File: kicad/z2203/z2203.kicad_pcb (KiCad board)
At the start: 4 copper layers, 80 x 80 mm, 21 parts, among them J1 Conn_01x01, J2 Conn_01x02, J3 Conn_02x20_Odd_Even, U13 LM4040AIM3-2.5, U14 AD5328, U15 M24C02-WMN, U7 PCA9555D

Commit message: routed z2203
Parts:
- removed C13, C25, C39: 0.1u, Capacitor_SMD:C_0603_1608Metric
- removed C24: 4.7u, Capacitor_SMD:C_0805_2012Metric
- removed R47: 4k7, Resistor_SMD:R_1206_3216Metric
- removed U13: LM4040AIM3-2.5, Package_TO_SOT_SMD:SOT-23
- removed U14: AD5328, Package_SO:TSSOP-16_4.4x5mm_P0.65mm
- added C1: 0.1u, Capacitor_SMD:C_0603_1608Metric, F.Cu at (77.2, 51.2)
- added C10: 0.1u, Capacitor_SMD:C_0603_1608Metric, F.Cu at (122.0, 59.0)
- added C2: 0.1u, Capacitor_SMD:C_0603_1608Metric, F.Cu at (92.4, 54.6)
- added C3: 0.1u, Capacitor_SMD:C_0603_1608Metric, F.Cu at (140.0, 76.3)
- added C4: 0.1u, Capacitor_SMD:C_0603_1608Metric, F.Cu at (142.2, 40.2)
- added C6: 0.1u, Capacitor_SMD:C_0603_1608Metric, F.Cu at (132.0, 52.4)
- added C7: 0.1u, Capacitor_SMD:C_0603_1608Metric, F.Cu at (76.6, 78.8)
- added C8: 0.1u, Capacitor_SMD:C_0603_1608Metric, F.Cu at (76.6, 66.8)
- added C9: 10u, Capacitor_SMD:C_0805_2012Metric, F.Cu at (79.0, 66.6)
- added D1: LED, LED_SMD:LED_0603_1608Metric, F.Cu at (143.6, 69.2)
- added R1: 4k7, Resistor_SMD:R_0603_1608Metric, F.Cu at (142.8, 72.8)
- added R2: 51, Resistor_SMD:R_0603_1608Metric, F.Cu at (79.0, 78.8)
- added R3: 47k, Resistor_SMD:R_0603_1608Metric, F.Cu at (74.0, 61.8)
- added R4: 47k, Resistor_SMD:R_0603_1608Metric, F.Cu at (74.0, 63.8)
- added R5: 47k, Resistor_SMD:R_0603_1608Metric, F.Cu at (74.0, 65.8)
- added R6: 47k, Resistor_SMD:R_0603_1608Metric, F.Cu at (71.4, 72.8)
- added R7: 47k, Resistor_SMD:R_0603_1608Metric, F.Cu at (73.8, 78.0)
- added R8: 51, Resistor_SMD:R_0603_1608Metric, F.Cu at (73.8, 80.0)
- added R9: 47k, Resistor_SMD:R_0603_1608Metric, F.Cu at (74.0, 67.6)
- added TP1: TestPoint, TestPoint:TestPoint_Pad_2.0x2.0mm, F.Cu at (121.2, 51.8)
- added TP11: TestPoint, TestPoint:TestPoint_Pad_2.0x2.0mm, F.Cu at (111.0, 52.2)
- added TP12: TestPoint, TestPoint:TestPoint_Pad_2.0x2.0mm, F.Cu at (69.2, 59.0)
- added TP2: TestPoint, TestPoint:TestPoint_Pad_2.0x2.0mm, F.Cu at (130.8, 48.4)
- added TP3: TestPoint, TestPoint:TestPoint_Pad_2.0x2.0mm, F.Cu at (131.8, 37.6)
- added TP4: TestPoint, TestPoint:TestPoint_Pad_2.0x2.0mm, F.Cu at (135.0, 64.4)
- added TP5: TestPoint, TestPoint:TestPoint_Pad_2.0x2.0mm, F.Cu at (139.1, 65.2)
- added TP6: TestPoint, TestPoint:TestPoint_Pad_2.0x2.0mm, F.Cu at (140.6, 50.9)
- added TP8: TestPoint, TestPoint:TestPoint_Pad_2.0x2.0mm, F.Cu at (136.8, 50.9)
- added TP9: TestPoint, TestPoint:TestPoint_Pad_2.0x2.0mm, F.Cu at (137.8, 79.8)
- added U1: YM2203, Package_DIP:DIP-40_W15.24mm, F.Cu at (126.3, 33.0)
- added U2: YM3014, Package_DIP:DIP-8_W7.62mm, F.Cu at (91.5, 57.0)
- added U3: 74HC595, Package_SO:TSSOP-16_4.4x5mm_P0.65mm, F.Cu at (137.2, 43.6)
- added U4: 74HC595, Package_SO:TSSOP-16_4.4x5mm_P0.65mm, F.Cu at (136.8, 71.0)
- added U6: TL074, Package_SO:TSSOP-14_4.4x5mm_P0.65mm, F.Cu at (76.4, 72.9)
- added X1: SX3M3.57, Oscillator:Oscillator_SMD_Abracon_ASE-4Pin_3.2x2.5mm, F.Cu at (122.0, 55.8)
- R56: value 2k -> 4k7
- U7: value PCA9555D -> 74HC00; footprint Package_SO:TSSOP-24_4.4x7.8mm_P0.65mm -> Package_SO:SOIC-14_3.9x8.7mm_P1.27mm
- moved J1 76.6 mm to (132.4, 28.6)
- moved G*** 76.3 mm to (69.4, 44.2), turned to 90 degrees
- moved D4 59.3 mm to (85.0, 27.7), turned to 180 degrees
- moved R56 57.3 mm to (88.7, 27.7), turned to 180 degrees
- moved U15 15.4 mm to (120.0, 78.5)
- moved C37 14.4 mm to (122.0, 84.4), turned to 90 degrees
- moved R20 8.86 mm to (142.2, 79.0)
- moved U7 5.65 mm to (136.8, 57.6), turned to 90 degrees
- moved J2 3.10 mm to (143.0, 83.3), turned to 0 degrees
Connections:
- D4 pad 1: Net-(D4-Pad1) -> Net-(D4-K)
- J3 pad 14: /GPIO_MODULE_DRIVEN -> unconnected-(J3-Pin_14-Pad14)
- J3 pad 21: /CARD1_OUT1 -> unconnected-(J3-Pin_21-Pad21)
- J3 pad 22: /CARD1_OUT2 -> unconnected-(J3-Pin_22-Pad22)
- J3 pad 23: /CARD2_OUT1 -> unconnected-(J3-Pin_23-Pad23)
- J3 pad 25: /CARD2_OUT2 -> unconnected-(J3-Pin_25-Pad25)
- J3 pad 26: /CARD3_OUT1 -> unconnected-(J3-Pin_26-Pad26)
- J3 pad 27: /CARD3_OUT2 -> unconnected-(J3-Pin_27-Pad27)
- J3 pad 29: /CARD4_OUT1 -> unconnected-(J3-Pin_29-Pad29)
- J3 pad 3: /SPI_MISO -> unconnected-(J3-Pin_3-Pad3)
- J3 pad 30: /CARD4_OUT2 -> unconnected-(J3-Pin_30-Pad30)
- J3 pad 31: /CARD5_OUT1 -> unconnected-(J3-Pin_31-Pad31)
- J3 pad 33: /CARD5_OUT2 -> unconnected-(J3-Pin_33-Pad33)
- J3 pad 34: /CARD6_OUT1 -> unconnected-(J3-Pin_34-Pad34)
- J3 pad 35: /CARD6_OUT2 -> unconnected-(J3-Pin_35-Pad35)
- J3 pad 37: /CARD7_OUT1 -> unconnected-(J3-Pin_37-Pad37)
- R56 pad 1: Net-(D4-Pad1) -> Net-(U1-IOA1)
- R56 pad 2: /LED_CTRL -> Net-(D4-K)
- U7 pad 1: unconnected-(U7-Pad1) -> +5V
- U7 pad 10: unconnected-(U7-Pad10) -> /CLK_CS1
- U7 pad 11: unconnected-(U7-Pad11) -> /CLK_CS1
- U7 pad 12: GND -> Net-(U7-Pad12)
- U7 pad 13: unconnected-(U7-Pad13) -> /SPI_CLK
- U7 pad 14: unconnected-(U7-Pad14) -> +5V
- U7 pad 2: /I2C_ADDR1 -> /SPI_CS1
- U7 pad 3: /I2C_ADDR2 -> Net-(U7-Pad12)
- U7 pad 7: /LED_CTRL -> GND
- U7 pad 8: unconnected-(U7-Pad8) -> /~CLK_CS1
- U7 pad 9: unconnected-(U7-Pad9) -> +5V
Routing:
- net +5V: track 21.5 -> 250.5 mm, vias 6 -> 11
- net /SPI_CS1: track 0.00 -> 74.7 mm
- net /YM2203_CLKS: track 0.00 -> 49.3 mm
- net -12V: track 0.00 -> 43.7 mm, vias 0 -> 1
- net +12V: track 0.00 -> 41.1 mm, vias 0 -> 1
- net /YM_CH_A: track 0.00 -> 38.1 mm
- net /YM_CH_B: track 0.00 -> 35.3 mm
- net /SPI_CS0: track 64.4 -> 30.4 mm
- net /YM_CH_C: track 0.00 -> 32.9 mm
- net /YM_D7: track 0.00 -> 31.3 mm
- net /YM_D6: track 0.00 -> 28.2 mm
- net /YM_A0: track 0.00 -> 27.9 mm, vias 0 -> 1
- net /YM_D5: track 0.00 -> 25.2 mm
- net Net-(U2-BUFF): track 0.00 -> 23.8 mm, vias 0 -> 1
- net /YM_D4: track 0.00 -> 22.4 mm
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- added copper zone on In2.Cu, net GND
- removed copper zone on In2.Cu, net +5V

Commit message: routed z2203
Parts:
- moved TP3 24.9 mm to (128.4, 70.0)
- moved C4 3.42 mm to (118.8, 57.8), turned to 90 degrees
- moved D1 0.19 mm to (85.2, 27.7)
- renumbered C3 to C10, C6 to C3, C10 to C4, C4 to C5, C9 to C6, C8 to C7, C7 to C8, C37 to C9, D4 to D1, D1 to D2, H4 to H1, H1 to H4, R56 to R1, R20 to R10, R1 to R11, R3 to R2, R8 to R3, R9 to R4, R4 to R5, R2 to R6, R5 to R8, R6 to R9, TP3 to TP1, TP9 to TP10, TP12 to TP2, TP11 to TP3, TP8 to TP4, TP1 to TP5, TP2 to TP6, TP6 to TP7, TP4 to TP8, TP5 to TP9, U7 to U3, U3 to U4, U6 to U5, U15 to U6, U4 to U7
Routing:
- net /YM2203_CLKS: track 49.3 -> 54.2 mm
- net +5V: track 250.5 -> 248.9 mm
- net Net-(U2-MP): track 19.2 -> 17.8 mm
- net GND: track 129.0 -> 127.8 mm
- net /SPI_CS1: track 74.7 -> 73.9 mm, vias 0 -> 1
- net /SPI_MOSI: track 60.9 -> 61.3 mm, vias 2 -> 0
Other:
- board text added: "TEST POINTS TP1 : YM D1 TP2 : YM CHANNEL A TP3 : SPI CS1 TP4 : CLK NAND CS1 TP5 : 3.57 MHZ CLK TP6 : YM D0 TP7 : CLK AND CS1 TP8 : YM A0 TP9 : SPI CS0 QB TP10 : SPI MOSI"
- board text added: "Z2203 FM SYNTH V0.1"

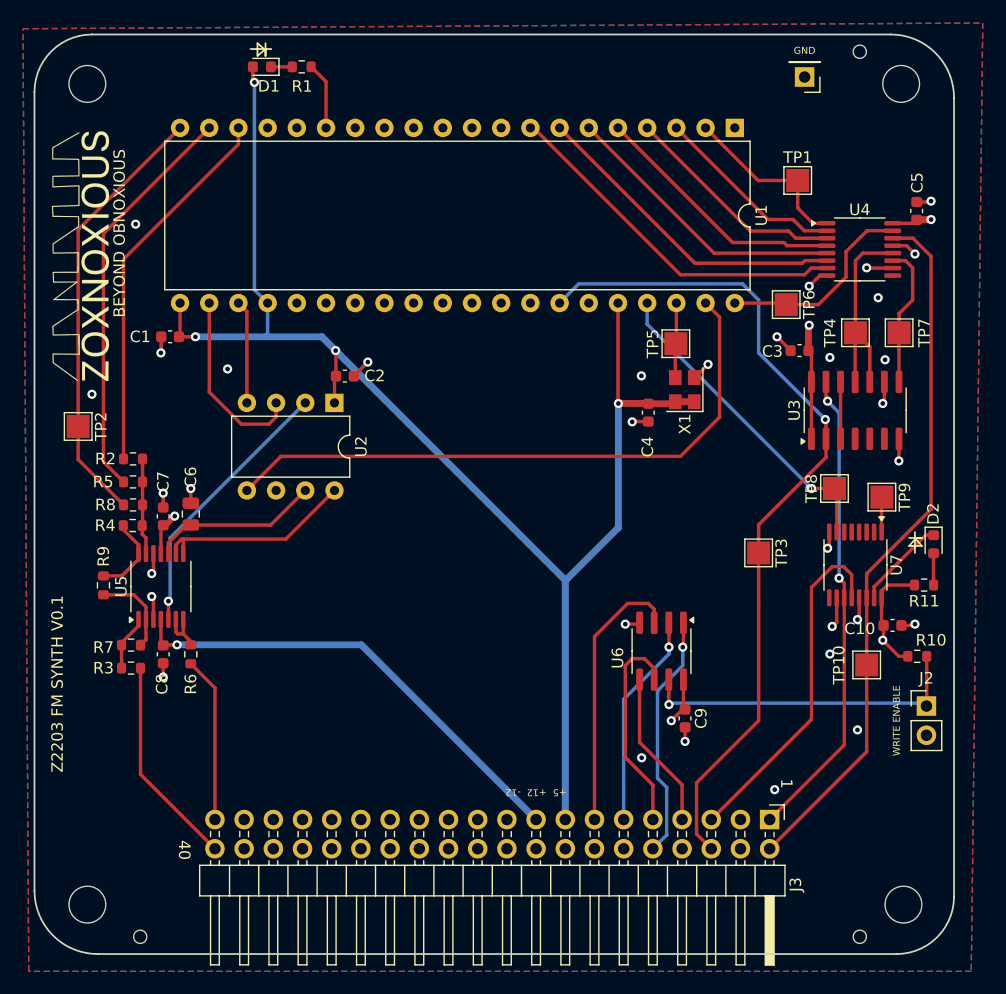
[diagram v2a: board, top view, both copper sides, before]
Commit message: move some stuff around for some minor changes.  The 2203 WR looks fine based on Capcom's Commando schematics
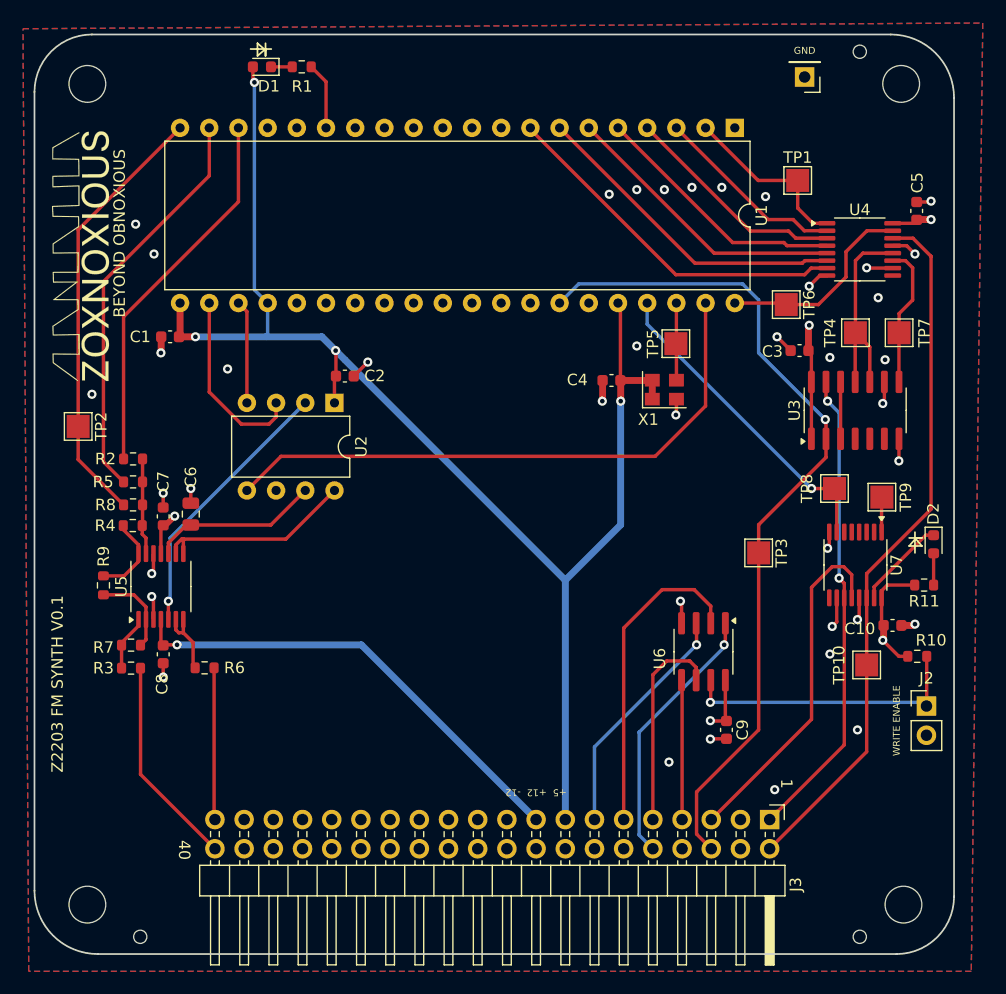
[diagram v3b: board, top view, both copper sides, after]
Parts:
- moved C4 4.25 mm to (115.6, 55.0), turned to 0 degrees
- moved C9 3.74 mm to (125.6, 85.4)
- moved U6 3.65 mm to (123.6, 78.6)
- moved X1 1.77 mm to (120.2, 55.8), turned to 0 degrees
- moved R6 1.68 mm to (80.2, 80.0), turned to 180 degrees
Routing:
- net /I2C_ADDR1: track 18.8 -> 27.7 mm, vias 1 -> 0
- net Net-(J2-Pin_1): track 29.0 -> 25.2 mm
- net /I2C_ADDR2: track 23.7 -> 20.8 mm, vias 0 -> 1
- net /YM2203_CLKS: track 54.2 -> 51.9 mm
- net Net-(U5B--): track 4.31 -> 6.30 mm
- net /I2C_ADDR0: track 21.4 -> 23.2 mm
- net /SDA1: track 13.7 -> 12.1 mm
- net /THIS_OUT1: track 14.4 -> 13.2 mm
- net GND: track 127.8 -> 128.8 mm, vias 30 -> 37
- net +5V: track 248.9 -> 248.1 mm

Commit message: silkscreen updates
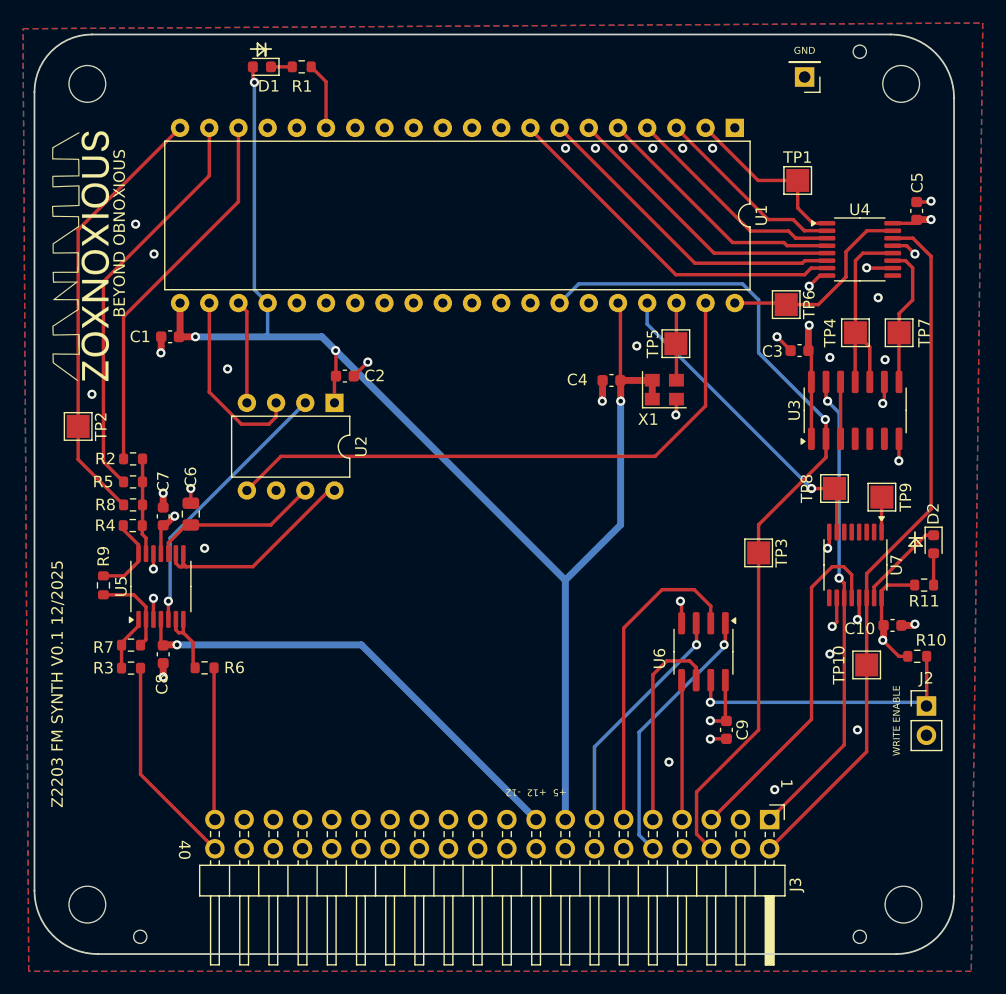
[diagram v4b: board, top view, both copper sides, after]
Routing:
- net Net-(U2-MP): track 17.8 -> 19.9 mm
- net GND: track 128.8 -> 128.1 mm, vias 37 -> 38
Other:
- board text added: "Z2203 FM SYNTH V0.1 12/2025"
- board text removed: "-12 +12 +5"
- board text removed: "Z2203 FM SYNTH V0.1"
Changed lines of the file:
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@@
   (gr_circle (center 137.2 103.4) (end 136.624 103.4)
     (stroke (width 0.05) (type solid)) (fill none) (layer "Edge.Cuts"))
-  (gr_text "-12  +12  +5" (at 108.635 90.85 180) (layer "B.SilkS")
-    (effects (font (size 0.6 0.6) (thickness 0.09)) (justify mirror))
-  )
   (gr_text "TEST POINTS\nTP1 : YM D1\nTP2 : YM CHANNEL A\nTP3 : SPI CS1\nTP4 : CLK NAND CS1\nTP5 : 3.57 MHZ CLK\nTP6 : YM D0\nTP7 : CLK AND CS1\nTP8 : YM A0\nTP9 :  SPI CS0 QB\nTP10 : SPI MOSI" (at 128.2 65) (layer "B.SilkS")
     (effects (font (size 0.8 0.8) (thickness 0.09)) (justify left bottom mirror))
   )
+  (gr_text "+5 +12 -12" (at 113.2 91) (layer "B.SilkS")
+    (effects (font (size 0.8 0.8) (thickness 0.09)) (justify left bottom mirror))
+  )
+  (gr_text "1" (at 130.8 91 -90) (layer "B.SilkS")
+    (effects (font (size 0.8 0.8) (thickness 0.09)) (justify left bottom mirror))
+  )
+  (gr_text "40" (at 77.8 96.8 270) (layer "B.SilkS")
+    (effects (font (size 0.8 0.8) (thickness 0.09)) (justify left bottom mirror))
+  )
   (gr_text "GND" (at 132.4 30.7) (layer "B.SilkS")
     (effects (font (size 0.6 0.6) (thickness 0.09)) (justify mirror))
   )
-  (gr_text "40" (at 78.435 95.85 270) (layer "B.SilkS")
-    (effects (font (size 0.6 0.6) (thickness 0.09)) (justify mirror))
-  )
-  (gr_text "1" (at 130.820001 90.079999 270) (layer "B.SilkS")
-    (effects (font (size 1 1) (thickness 0.15)) (justify mirror))
-  )
   (gr_text "+5  +12  -12" (at 109.035 90.85 180) (layer "F.SilkS")
     (effects (font (size 0.6 0.6) (thickness 0.09)))
@@
     (effects (font (size 1 1) (thickness 0.15)))
   )
-  (gr_text "Z2203 FM SYNTH V0.1" (at 67.4 81.4 90) (layer "F.SilkS")
+  (gr_text "Z2203 FM SYNTH V0.1 12/2025" (at 67.4 81.4 90) (layer "F.SilkS")
     (effects (font (size 1 1) (thickness 0.09)))
   )
@@
     (effects (font (size 0.6 0.6) (thickness 0.09)))
   )
+  (segment (start 75.75 71.4) (end 75.75 70.0625) (width 0.3) (layer "F.Cu") (net 1))
   (segment (start 134.4 69.6) (end 134.5475 69.4525) (width 0.3) (layer "F.Cu") (net 1))
   (segment (start 125.6 86.175) (end 124.225 86.175) (width 0.3) (layer "F.Cu") (net 1))
@@
   (segment (start 133.725 45.875) (end 134.3375 45.875) (width 0.3) (layer "F.Cu") (net 1))
   (segment (start 140.8225 76.3125) (end 141.8875 76.3125) (width 0.6) (layer "F.Cu") (net 1))
-  (segment (start 76.6 66.05) (end 76.6 64.8) (width 0.3) (layer "F.Cu") (net 1))
+  (segment (start 76.6 66.05) (end 76.6 64.8) (width 0.6) (layer "F.Cu") (net 1))
   (segment (start 76.425 51.2) (end 76.425 52.575) (width 0.6) (layer "F.Cu") (net 1))
+  (segment (start 140.61 60.075) (end 140.61 61.99) (width 0.3) (layer "F.Cu") (net 1))
   (segment (start 75.75 73.95) (end 75.75 75.7875) (width 0.3) (layer "F.Cu") (net 1))
-  (segment (start 140.61 60.075) (end 140.61 61.99) (width 0.3) (layer "F.Cu") (net 1))
   (segment (start 131.185 52.385) (end 131.185 52.4) (width 0.3) (layer "F.Cu") (net 1))
   (segment (start 143.325 39.475) (end 143.4 39.4) (width 0.3) (layer "F.Cu") (net 1))
-  (segment (start 75.75 70.0625) (end 75.75 71.65) (width 0.3) (layer "F.Cu") (net 1))
   (segment (start 93.18 54.62) (end 94.4 53.4) (width 0.3) (layer "F.Cu") (net 1))
   (segment (start 140.61 61.99) (end 140.6 62) (width 0.3) (layer "F.Cu") (net 1))
-  (segment (start 75.75 71.65) (end 75.6 71.8) (width 0.3) (layer "F.Cu") (net 1))
   (segment (start 121.695 76.125) (end 121.695 74.295) (width 0.3) (layer "F.Cu") (net 1))
   (segment (start 140.0625 43.275) (end 141.275 43.275) (width 0.3) (layer "F.Cu") (net 1))
@@
   (segment (start 137.1475 73.9125) (end 137.1475 75.6525) (width 0.3) (layer "F.Cu") (net 1))
   (segment (start 76.425 52.575) (end 76.4 52.6) (width 0.3) (layer "F.Cu") (net 1))
-  (segment (start 76.6 79.6) (end 76.6 80.8) (width 0.3) (layer "F.Cu") (net 1))
+  (segment (start 76.6 79.6) (end 76.6 80.8) (width 0.6) (layer "F.Cu") (net 1))
   (segment (start 137.1475 75.6525) (end 137 75.8) (width 0.3) (layer "F.Cu") (net 1))
   (segment (start 114.825 55) (end 114.825 56.775) (width 0.6) (layer "F.Cu") (net 1))
@@
   (segment (start 130 51.2) (end 131.185 52.385) (width 0.3) (layer "F.Cu") (net 1))
   (segment (start 132.8 46.8) (end 133.725 45.875) (width 0.3) (layer "F.Cu") (net 1))
-  (segment (start 75.6 73.8) (end 75.75 73.95) (width 0.3) (layer "F.Cu") (net 1))
-  (via (at 117.8 38.4) (size 0.8) (drill 0.4) (layers "F.Cu" "B.Cu") (net 1))
-  (via (at 75.6 71.8) (size 0.8) (drill 0.4) (layers "F.Cu" "B.Cu") (net 1))
-  (via (at 120.2 38.4) (size 0.8) (drill 0.4) (layers "F.Cu" "B.Cu") (net 1))
-  (via (at 125.2 38.2) (size 0.8) (drill 0.4) (layers "F.Cu" "B.Cu") (net 1))
+  (via (at 114.2 34.8) (size 0.8) (drill 0.4) (layers "F.Cu" "B.Cu") (net 1))
+  (via (at 75.75 71.4) (size 0.8) (drill 0.4) (layers "F.Cu" "B.Cu") (net 1))
+  (via (at 116.6 34.8) (size 0.8) (drill 0.4) (layers "F.Cu" "B.Cu") (net 1))
+  (via (at 121.8 34.8) (size 0.8) (drill 0.4) (layers "F.Cu" "B.Cu") (net 1))
   (via (at 94.4 53.4) (size 0.8) (drill 0.4) (layers "F.Cu" "B.Cu") (net 1))
   (via (at 124.2 86.2) (size 0.8) (drill 0.4) (layers "F.Cu" "B.Cu") (net 1))
@@
   (via (at 137 75.8) (size 0.8) (drill 0.4) (layers "F.Cu" "B.Cu") (net 1))
   (via (at 70.4 56.2) (size 0.8) (drill 0.4) (layers "F.Cu" "B.Cu") (net 1))
-  (via (at 129 39) (size 0.8) (drill 0.4) (layers "F.Cu" "B.Cu") (net 1))
+  (via (at 124.4 34.8) (size 0.8) (drill 0.4) (layers "F.Cu" "B.Cu") (net 1))
   (via (at 137 85.4) (size 0.8) (drill 0.4) (layers "F.Cu" "B.Cu") (net 1))
   (via (at 138.8 47.8) (size 0.8) (drill 0.4) (layers "F.Cu" "B.Cu") (net 1))
@@
   (via (at 142 44) (size 0.8) (drill 0.4) (layers "F.Cu" "B.Cu") (net 1))
   (via (at 130 51.2) (size 0.8) (drill 0.4) (layers "F.Cu" "B.Cu") (net 1))
-  (via (at 75.6 73.8) (size 0.8) (drill 0.4) (layers "F.Cu" "B.Cu") (net 1))
+  (via (at 80.2 69.6) (size 0.8) (drill 0.4) (layers "F.Cu" "B.Cu") (net 1))
+  (via (at 75.75 73.95) (size 0.8) (drill 0.4) (layers "F.Cu" "B.Cu") (net 1))
   (via (at 79 64.4) (size 0.8) (drill 0.4) (layers "F.Cu" "B.Cu") (net 1))
   (via (at 74.2 41.4) (size 0.8) (drill 0.4) (layers "F.Cu" "B.Cu") (net 1))
   (via (at 82.2 54) (size 0.8) (drill 0.4) (layers "F.Cu" "B.Cu") (net 1))
-  (via (at 122.6 38.2) (size 0.8) (drill 0.4) (layers "F.Cu" "B.Cu") (net 1))
-  (via (at 115.4 38.8) (size 0.8) (drill 0.4) (layers "F.Cu" "B.Cu") (net 1))
+  (via (at 119.2 34.8) (size 0.8) (drill 0.4) (layers "F.Cu" "B.Cu") (net 1))
+  (via (at 111.6 34.8) (size 0.8) (drill 0.4) (layers "F.Cu" "B.Cu") (net 1))
   (via (at 132.8 46.8) (size 0.8) (drill 0.4) (layers "F.Cu" "B.Cu") (net 1))
   (via (at 121.2 58) (size 0.8) (drill 0.4) (layers "F.Cu" "B.Cu") (net 1))
@@
   (segment (start 78.6125 67.575) (end 79 67.575) (width 0.3) (layer "F.Cu") (net 3))
   (segment (start 77.05 70.0625) (end 77.05 69.1375) (width 0.3) (layer "F.Cu") (net 3))
-  (segment (start 77.8 78) (end 76.65 78) (width 0.3) (layer "F.Cu") (net 4))
+  (segment (start 77.8 78) (end 76.65 78) (width 0.6) (layer "F.Cu") (net 4))
   (segment (start 76.65 78) (end 76.6 78.05) (width 0.3) (layer "F.Cu") (net 4))
   (segment (start 76.4 75.7875) (end 76.4 77.85) (width 0.3) (layer "F.Cu") (net 4))
@@
   (segment (start 77.2 68.71) (end 88.96 56.95) (width 0.3) (layer "B.Cu") (net 66))
   (segment (start 77.2 74.05) (end 77.2 68.71) (width 0.3) (layer "B.Cu") (net 66))
-  (segment (start 78.2 68.8) (end 78.4 68.8) (width 0.3) (layer "F.Cu") (net 67))
-  (segment (start 78.4 68.8) (end 87.27 68.8) (width 0.3) (layer "F.Cu") (net 67))
-  (segment (start 87.27 68.8) (end 91.5 64.57) (width 0.3) (layer "F.Cu") (net 67))
-  (segment (start 77.7 69.3) (end 78.2 68.8) (width 0.3) (layer "F.Cu") (net 67))
-  (segment (start 78.35 70.0625) (end 78.35 68.85) (width 0.3) (layer "F.Cu") (net 67))
-  (segment (start 78.35 68.85) (end 78.4 68.8) (width 0.3) (layer "F.Cu") (net 67))
-  (segment (start 77.7 70.0625) (end 77.7 69.3) (width 0.3) (layer "F.Cu") (net 67))
+  (segment (start 91.03 64.57) (end 84.4 71.2) (width 0.3) (layer "F.Cu") (net 67))
+  (segment (start 78.6 71.2) (end 78.2 71.2) (width 0.3) (layer "F.Cu") (net 67))
+  (segment (start 78.35 70.0625) (end 78.35 70.95) (width 0.3) (layer "F.Cu") (net 67))
+  (segment (start 91.5 64.57) (end 91.03 64.57) (width 0.3) (layer "F.Cu") (net 67))
+  (segment (start 78.2 71.2) (end 78 71.2) (width 0.3) (layer "F.Cu") (net 67))
+  (segment (start 78.35 71.05) (end 78.2 71.2) (width 0.3) (layer "F.Cu") (net 67))
+  (segment (start 78 71.2) (end 77.7 70.9) (width 0.3) (layer "F.Cu") (net 67))
+  (segment (start 84.4 71.2) (end 78.6 71.2) (width 0.3) (layer "F.Cu") (net 67))
+  (segment (start 78.35 70.95) (end 78.6 71.2) (width 0.3) (layer "F.Cu") (net 67))
+  (segment (start 78.35 70.0625) (end 78.35 71.05) (width 0.3) (layer "F.Cu") (net 67))
+  (segment (start 77.7 70.9) (end 77.7 70.0625) (width 0.3) (layer "F.Cu") (net 67))
   (segment (start 139.0975 65.175) (end 139.1225 65.15) (width 0.3) (layer "F.Cu") (net 68))
   (segment (start 139.0975 68.1875) (end 139.0975 65.175) (width 0.3) (layer "F.Cu") (net 68))
